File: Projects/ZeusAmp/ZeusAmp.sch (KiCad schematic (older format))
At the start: 58 parts, among them Q1 NZT660, Q11 NZT660, Q12 NZT660, Q121 NZT660, Q2 NZT660, Q21 NZT660, Q3 PZTA06, Q31 PZTA06, Q4 MJD340T4, Q41 MJD340T4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

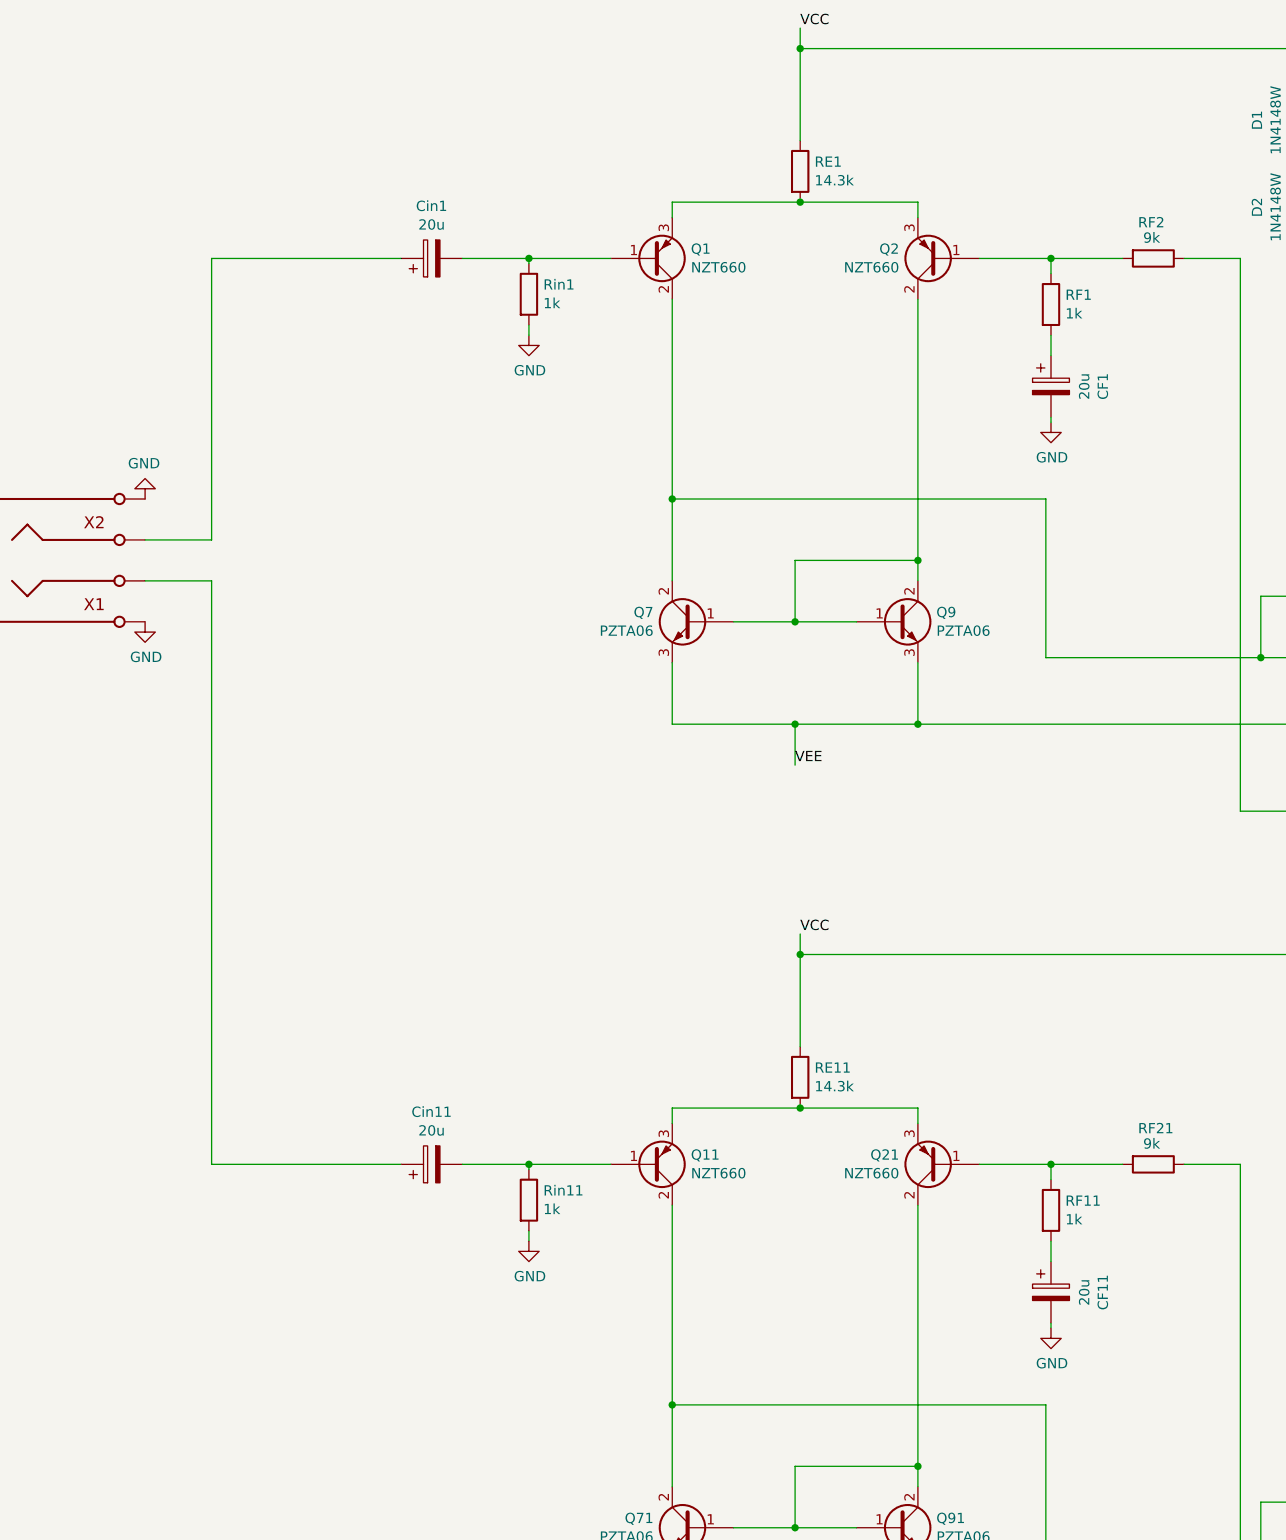
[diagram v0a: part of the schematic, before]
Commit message: completed full layout, needs volume control pot and +-15V rails
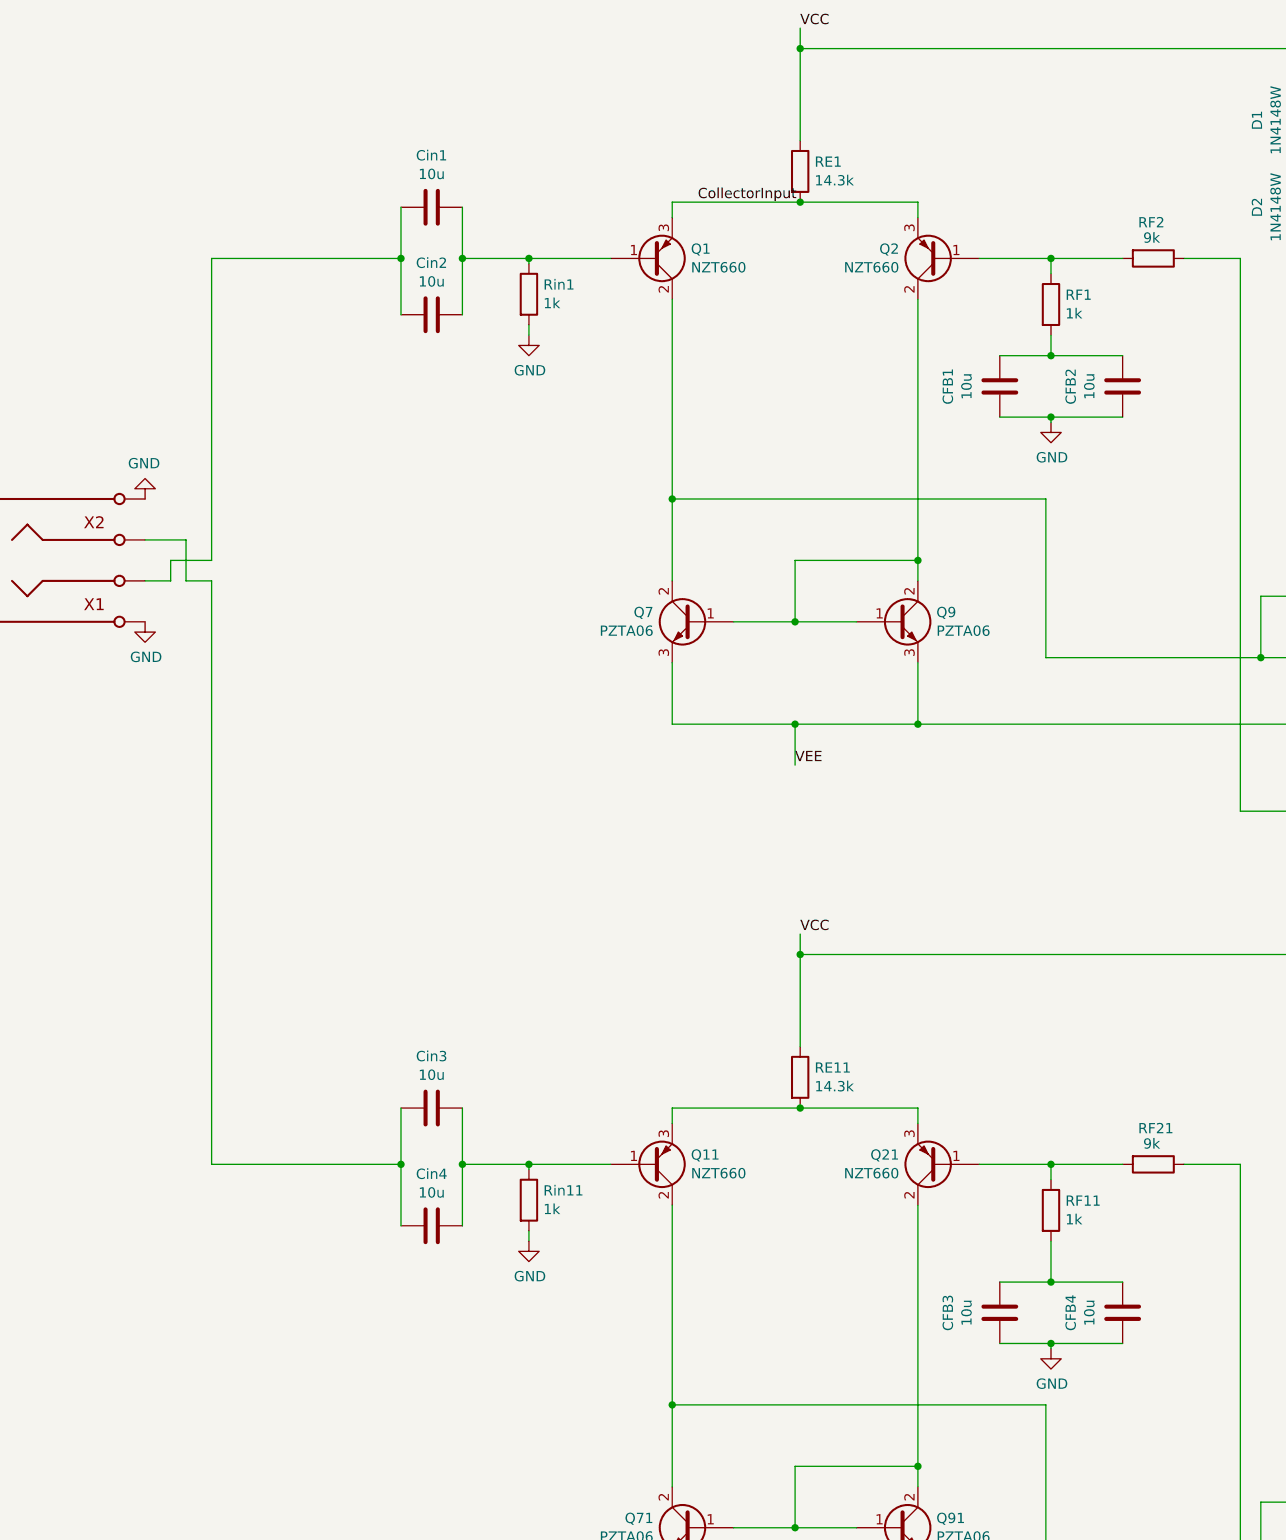
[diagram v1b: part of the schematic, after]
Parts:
- removed CF1, CF11, Cin1, Cin11: 20u, Capacitor_THT:CP_Radial_D10.0mm_P5.00mm, symbol Device:CP
- added CFB1, CFB2, CFB3, CFB4, Cin1, Cin2, Cin3, Cin4: 10u, Capacitor_SMD:C_0805_2012Metric, symbol Device:C
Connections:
- net GND: now also CFB1.1, CFB2.1, CFB3.1, CFB4.1
- net at Q1.1 (B), Rin1.1: now also Cin1.2, Cin2.2
- net CollectorInput: now reaches Q1.3 (E), Q2.3 (E), RE1.2
- net at Jin1.4: now also Cin3.1, Cin4.1
- net at Jin1.2: now also Cin1.1, Cin2.1
- net at RF1.2: now also CFB1.2, CFB2.2
- net at Q11.1 (B), Rin11.1: now also Cin3.2, Cin4.2
- net at RF11.2: now also CFB3.2, CFB4.2
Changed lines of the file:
@@
 Wire Wire Line
 	3300 2250 3700 2250
-$Comp
-L Device:CP Cin1
-U 1 1 604A684C
-P 2825 2250
-F 0 "Cin1" V 3080 2250 50  0000 C CNN
-F 1 "20u" V 2989 2250 50  0000 C CNN
-F 2 "Capacitor_THT:CP_Radial_D10.0mm_P5.00mm" H 2863 2100 50  0001 C CNN
-F 3 "~" H 2825 2250 50  0001 C CNN
-	1    2825 2250
-	0    -1   -1   0
-$EndComp
 Wire Wire Line
 	2975 2250 3300 2250
@@
 	1    0    0    -1
 $EndComp
-$Comp
-L Device:CP CF1
-U 1 1 604B23DC
-P 5850 2875
-F 0 "CF1" V 6105 2875 50  0000 C CNN
-F 1 "20u" V 6014 2875 50  0000 C CNN
-F 2 "Capacitor_THT:CP_Radial_D10.0mm_P5.00mm" H 5888 2725 50  0001 C CNN
-F 3 "~" H 5850 2875 50  0001 C CNN
-	1    5850 2875
-	1    0    0    -1
-$EndComp
 Wire Wire Line
 	5850 2625 5850 2725
@@
 $EndComp
 Wire Wire Line
-	1750 3625 1425 3625
-Wire Wire Line
-	1750 2250 1750 3625
-Wire Wire Line
 	1750 2250 2675 2250
 $Comp
@@
 Wire Wire Line
 	3300 6675 3700 6675
-$Comp
-L Device:CP Cin11
-U 1 1 60594D59
-P 2825 6675
-F 0 "Cin11" V 3080 6675 50  0000 C CNN
-F 1 "20u" V 2989 6675 50  0000 C CNN
-F 2 "Capacitor_THT:CP_Radial_D10.0mm_P5.00mm" H 2863 6525 50  0001 C CNN
-F 3 "~" H 2825 6675 50  0001 C CNN
-	1    2825 6675
-	0    -1   -1   0
-$EndComp
 Wire Wire Line
 	2975 6675 3300 6675
@@
 	1    0    0    -1
 $EndComp
-$Comp
-L Device:CP CF11
-U 1 1 60594D72
-P 5850 7300
-F 0 "CF11" V 6105 7300 50  0000 C CNN
-F 1 "20u" V 6014 7300 50  0000 C CNN
-F 2 "Capacitor_THT:CP_Radial_D10.0mm_P5.00mm" H 5888 7150 50  0001 C CNN
-F 3 "~" H 5850 7300 50  0001 C CNN
-	1    5850 7300
-	1    0    0    -1
-$EndComp
-Wire Wire Line
-	5850 7050 5850 7150
-$Comp
-L power:GND #PWR0107
-U 1 1 60594D79
-P 5850 7475
-F 0 "#PWR0107" H 5850 7225 50  0001 C CNN
-F 1 "GND" H 5855 7302 50  0000 C CNN
-F 2 "" H 5850 7475 50  0001 C CNN
-F 3 "" H 5850 7475 50  0001 C CNN
-	1    5850 7475
-	1    0    0    -1
-$EndComp
-Wire Wire Line
-	5850 7475 5850 7450
 Wire Wire Line
 	5500 6675 5850 6675
@@
 RightAudioChannel
 Wire Wire Line
-	1425 3825 1750 3825
-Wire Wire Line
 	1750 3825 1750 6675
 $Comp
@@
 	-1   0    0    1
 $EndComp
+$Comp
+L Device:C Cin1
+U 1 1 604ADA3C
+P 2825 2000
+F 0 "Cin1" V 3077 2000 50  0000 C CNN
+F 1 "10u" V 2986 2000 50  0000 C CNN
+F 2 "Capacitor_SMD:C_0805_2012Metric" H 2863 1850 50  0001 C CNN
+F 3 "~" H 2825 2000 50  0001 C CNN
+	1    2825 2000
+	0    -1   -1   0
+$EndComp
+$Comp
+L Device:C Cin2
+U 1 1 604B6691
+P 2825 2525
+F 0 "Cin2" V 3077 2525 50  0000 C CNN
+F 1 "10u" V 2986 2525 50  0000 C CNN
+F 2 "Capacitor_SMD:C_0805_2012Metric" H 2863 2375 50  0001 C CNN
+F 3 "~" H 2825 2525 50  0001 C CNN
+	1    2825 2525
+	0    -1   -1   0
+$EndComp
+Wire Wire Line
+	2675 2000 2675 2250
+Connection ~ 2675 2250
+Wire Wire Line
+	2675 2250 2675 2525
+Wire Wire Line
+	2975 2000 2975 2250
+Connection ~ 2975 2250
+Wire Wire Line
+	2975 2250 2975 2525
+$Comp
+L Device:C CFB2
+U 1 1 604C74BB
+P 6200 2875
+F 0 "CFB2" V 6452 2875 50  0000 C CNN
+F 1 "10u" V 6361 2875 50  0000 C CNN
+F 2 "Capacitor_SMD:C_0805_2012Metric" H 6238 2725 50  0001 C CNN
+F 3 "~" H 6200 2875 50  0001 C CNN
+	1    6200 2875
+	-1   0    0    1
+$EndComp
+$Comp
+L Device:C CFB1
+U 1 1 604D03D1
+P 5600 2875
+F 0 "CFB1" V 5852 2875 50  0000 C CNN
+F 1 "10u" V 5761 2875 50  0000 C CNN
+F 2 "Capacitor_SMD:C_0805_2012Metric" H 5638 2725 50  0001 C CNN
+F 3 "~" H 5600 2875 50  0001 C CNN
+	1    5600 2875
+	-1   0    0    1
+$EndComp
+Connection ~ 5850 3025
+Wire Wire Line
+	5850 3025 5600 3025
+Wire Wire Line
+	6200 3025 5850 3025
+Wire Wire Line
+	5600 2725 5850 2725
+Connection ~ 5850 2725
+Wire Wire Line
+	5850 2725 6200 2725
+$Comp
+L Device:C Cin3
+U 1 1 604FD973
+P 2825 6400
+F 0 "Cin3" V 3077 6400 50  0000 C CNN
+F 1 "10u" V 2986 6400 50  0000 C CNN
+F 2 "Capacitor_SMD:C_0805_2012Metric" H 2863 6250 50  0001 C CNN
+F 3 "~" H 2825 6400 50  0001 C CNN
+	1    2825 6400
+	0    -1   -1   0
+$EndComp
+$Comp
+L Device:C Cin4
+U 1 1 604FE61D
+P 2825 6975
+F 0 "Cin4" V 3077 6975 50  0000 C CNN
+F 1 "10u" V 2986 6975 50  0000 C CNN
+F 2 "Capacitor_SMD:C_0805_2012Metric" H 2863 6825 50  0001 C CNN
+F 3 "~" H 2825 6975 50  0001 C CNN
+	1    2825 6975
+	0    -1   -1   0
+$EndComp
+Wire Wire Line
+	2675 6400 2675 6675
+Connection ~ 2675 6675
+Wire Wire Line
+	2675 6675 2675 6975
+Wire Wire Line
+	2975 6975 2975 6675
+Connection ~ 2975 6675
+Wire Wire Line
+	2975 6675 2975 6400
+$Comp
+L power:GND #PWR0107
+U 1 1 60517FE1
+P 5850 7575
+F 0 "#PWR0107" H 5850 7325 50  0001 C CNN
+F 1 "GND" H 5855 7402 50  0000 C CNN
+F 2 "" H 5850 7575 50  0001 C CNN
+F 3 "" H 5850 7575 50  0001 C CNN
+	1    5850 7575
+	1    0    0    -1
+$EndComp
+Wire Wire Line
+	5850 7575 5850 7550
+$Comp
+L Device:C CFB4
+U 1 1 60517FE8
+P 6200 7400
+F 0 "CFB4" V 6452 7400 50  0000 C CNN
+F 1 "10u" V 6361 7400 50  0000 C CNN
+F 2 "Capacitor_SMD:C_0805_2012Metric" H 6238 7250 50  0001 C CNN
+F 3 "~" H 6200 7400 50  0001 C CNN
+	1    6200 7400
+	-1   0    0    1
+$EndComp
+$Comp
+L Device:C CFB3
+U 1 1 60517FEE
+P 5600 7400
+F 0 "CFB3" V 5852 7400 50  0000 C CNN
+F 1 "10u" V 5761 7400 50  0000 C CNN
+F 2 "Capacitor_SMD:C_0805_2012Metric" H 5638 7250 50  0001 C CNN
+F 3 "~" H 5600 7400 50  0001 C CNN
+	1    5600 7400
+	-1   0    0    1
+$EndComp
+Connection ~ 5850 7550
+Wire Wire Line
+	5850 7550 5600 7550
+Wire Wire Line
+	6200 7550 5850 7550
+Wire Wire Line
+	5600 7250 5850 7250
+Connection ~ 5850 7250
+Wire Wire Line
+	5850 7250 6200 7250
+Wire Wire Line
+	5850 7050 5850 7250
+Text Label 4125 1975 0    50   ~ 0
+CollectorInput
+Wire Wire Line
+	1750 3825 1625 3825
+Wire Wire Line
+	1625 3825 1625 3625
+Wire Wire Line
+	1625 3625 1425 3625
+Wire Wire Line
+	1750 3725 1550 3725
+Wire Wire Line
+	1550 3725 1550 3825
+Wire Wire Line
+	1550 3825 1425 3825
+Wire Wire Line
+	1750 2250 1750 3725
 $EndSCHEMATC

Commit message: First Zeus V1 completed
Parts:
- added 16VACIn1: Barrel_Jack, Connector_BarrelJack:BarrelJack_Horizontal, symbol Connector:Barrel_Jack
- added CPower1, CPower11: 1000u, Capacitor_THT:CP_Radial_D13.0mm_P5.00mm, symbol Device:CP
- added CPower2: 10u, Capacitor_SMD:C_0805_2012Metric, symbol Device:C
- added CPower22, CPower3, CPower5: 10u, Capacitor_Tantalum_SMD:CP_EIA-6032-28_Kemet-C, symbol Device:CP
- added DP1, DP2: 1N4148W, Diode_SMD:D_SOD-123, symbol Diode:1N4148W
- added RV1: R_POT_Dual, Potentiometer_THT:Potentiometer_Alps_RK09L_Double_Vertical, symbol Device:R_POT_Dual
- added U5: LM2990S-15_NOPB, Package_TO_SOT_SMD:TO-263-3_TabPin2, symbol AdditionalParts:LM2990S-15_NOPB
- added U6: LM2937ESX-15_NOPB, Package_TO_SOT_SMD:TO-263-3_TabPin2, symbol AdditionalParts:LM2937ESX-15_NOPB
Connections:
- net GND: now also CPower1.2, CPower11.1, CPower2.2, CPower22.1, CPower3.1, CPower5.1, RV1.1, RV1.6, U5.1 (GND), U6.2 (GND)
- net VCC: now also CPower3.2, U6.3 (Out)
- net VEE: now also CPower5.2, U5.3 (Out)
- net at Cin1.1, Cin2.1: now also RV1.2; no longer Jin1.2
- net at Cin3.1, Cin4.1: now also RV1.5; no longer Jin1.4
- new net: Jin1.2, RV1.3
- new net: Jin1.4, RV1.4
- new net: CPower11.2, CPower22.2, DP1.2 (A), U5.2 (In)
- new net: CPower1.1, CPower2.1, DP2.1 (K), U6.1 (In)
- new net V+: 16VACIn1.1, DP2.2 (A)
- new net V-: 16VACIn1.2, DP1.1 (K)

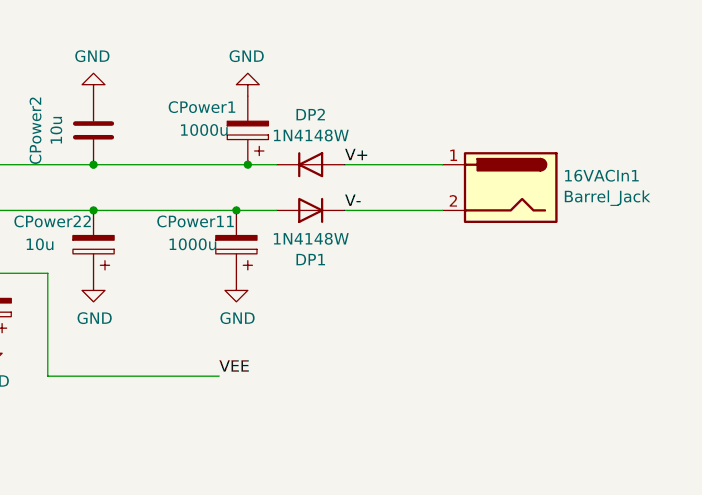
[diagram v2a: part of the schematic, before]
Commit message: Fixed Power Supply Issue
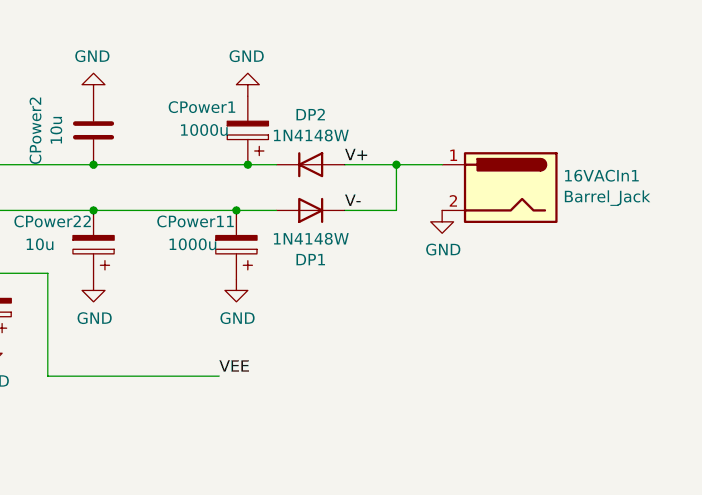
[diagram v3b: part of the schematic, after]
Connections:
- net GND: now also 16VACIn1.2
- net V+: now also DP1.1 (K)
- removed net V-: 16VACIn1.2, DP1.1 (K)
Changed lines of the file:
@@
 $EndComp
 Wire Wire Line
-	13625 1225 13200 1225
-Wire Wire Line
-	13625 1425 13200 1425
+	13625 1225 13425 1225
 Text Label 13200 1225 0    50   ~ 0
 V+
@@
 Text Label 10350 850  0    50   ~ 0
 VCC
+$Comp
+L power:GND #PWR?
+U 1 1 604C2102
+P 13625 1425
+F 0 "#PWR?" H 13625 1175 50  0001 C CNN
+F 1 "GND" H 13630 1252 50  0000 C CNN
+F 2 "" H 13625 1425 50  0001 C CNN
+F 3 "" H 13625 1425 50  0001 C CNN
+	1    13625 1425
+	1    0    0    -1
+$EndComp
+Wire Wire Line
+	13425 1225 13425 1425
+Wire Wire Line
+	13200 1425 13425 1425
+Connection ~ 13425 1225
+Wire Wire Line
+	13425 1225 13200 1225
 $EndSCHEMATC
